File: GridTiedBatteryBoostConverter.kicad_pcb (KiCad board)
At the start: 2 copper layers, 270.1 x 143.1 mm, 161 parts, among them J101 Battery Connection, J103 Solar Panels, J202 Conn_01x03_Female, J203 I2C_BUS, J401 Screw_Terminal_01x02, J402 AudioJack2_SwitchT, Q101 IXFP36N20X3, Q102 BC847B-13-F, Q103 SSM3K329R, Q104 SSM3J334R, Q201 SSM3K329R, Q202 SSM3K329R, Q203 SSM3J334R, Q301 BC847B-13-F, Q302 BC856B-13-F, Q305 TK32A12N1,S4X, Q306 TK32A12N1,S4X, SW201 SW_Up, SW202 SW_Down, SW203 SW_Enter, U101 OPA2837DGK, U102 UCC2800DTR, U201 LCD 2004A, U202 Teensy-LC, U203 PCF8574ADWR, U204 ESP-WROOM-02U, U301 FDA217, U302 LTC7138EMSE-PBF, U303 TPS560200, U304 TLV70430_SOT23-5, U305 REF2925AIDBZT, U306 TPS560200

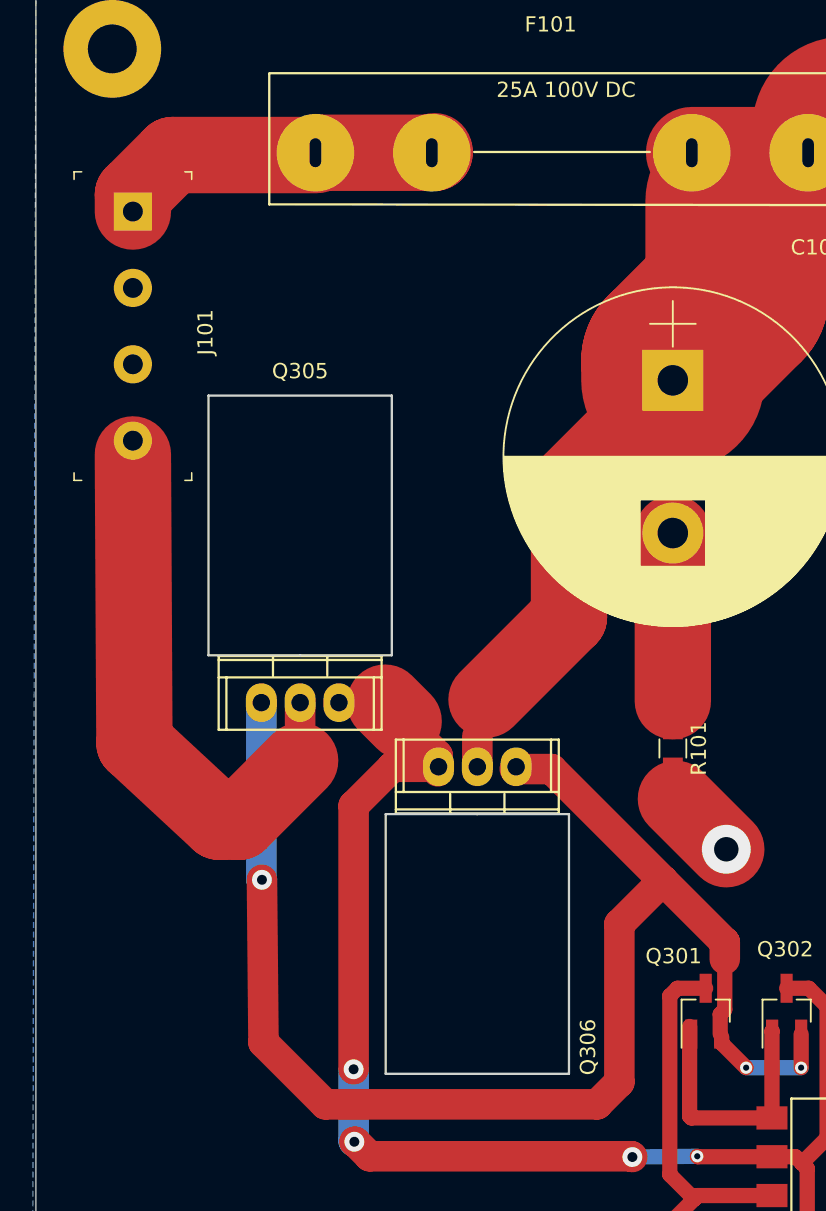
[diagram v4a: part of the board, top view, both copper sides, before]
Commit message: change Fuse details to a graphic note, and change the Fuse supply details to refer to the fuse holder, not the fuse it self.  Also rerouted the charger input using 8mm trace width were possible.
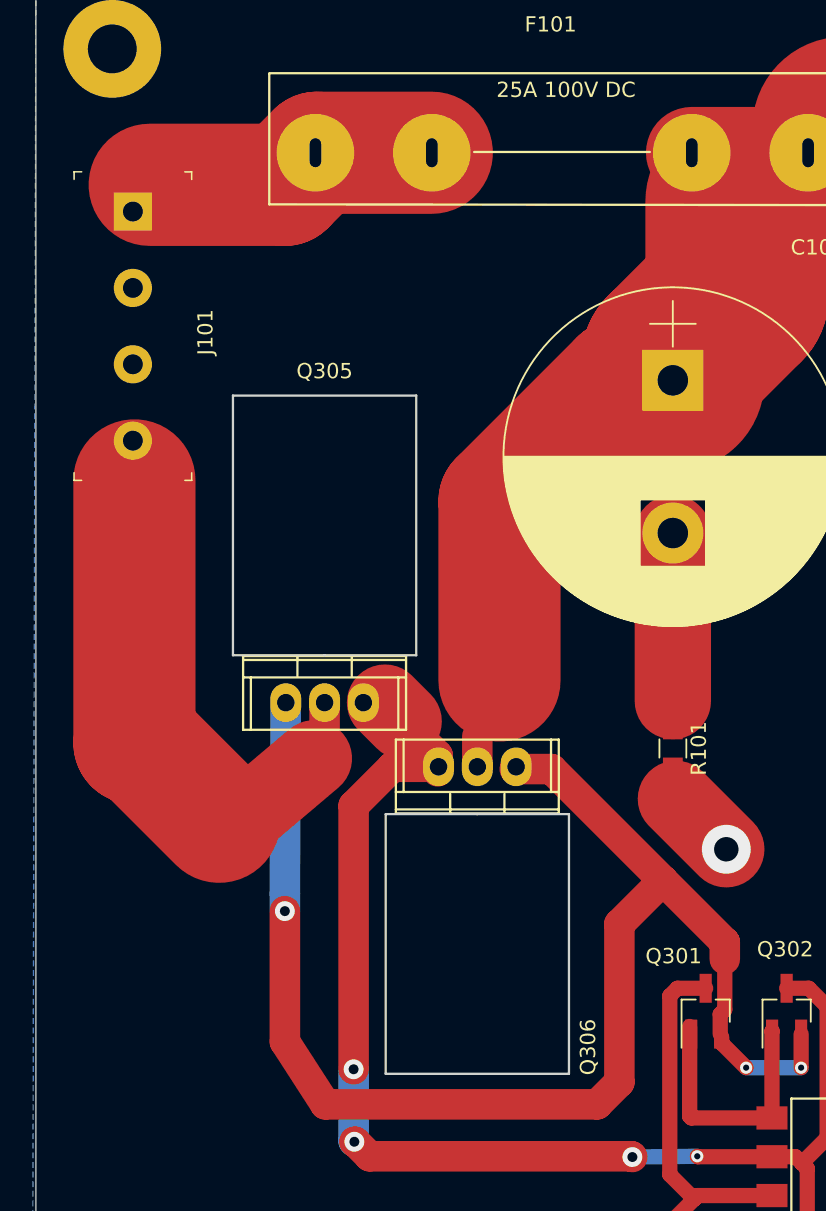
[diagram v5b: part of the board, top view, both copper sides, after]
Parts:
- moved Q305 1.60 mm to (31.9, 62.3)
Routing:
- net Net-(C314-Pad2): track 93.5 -> 90.5 mm
- net Net-(F101-Pad1): track 22.2 -> 19.6 mm
- net ChargerConnection: track 35.2 -> 36.5 mm
- net Net-(Q301-Pad2): track 98.0 -> 97.3 mm

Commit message: added labels for the battery, charger, inverter and solar panels + - connections.
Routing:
- net Vin: track 240.5 -> 244.7 mm
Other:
- board text added: "+ Bat -"
- board text added: "+ Solar Panels -"
- board text added: "- Charger +"

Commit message: Started making progress towards people being able to clone the the repository without getting messages about missing librarys needing rescue. started simplifying where some component librarys are located.
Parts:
- C101: value 220uF 200V 905 mOhm -> 220uF ALUM 200V 905 mOhm 20%
- C102: value 15uF 250VDC 3.9mOhm -> 15uF PP 250VDC 3.9mOhm
- C103: value 470uF 400V 130mOhm -> 470uF ALUM 400V 130mOhm 20%
- C204, C301, C305, C307, C308, C310, C311: value 10uF X7R 16V -> 10uF X7R 25V 10%
- C303, C314: value 1uF X7R 250V -> 1uF X7R 250V 10%
- C306, C315: value 33uF X7R 16V -> 33uF X7R 16V 20%
- D101: value 8A 200V 0.950V fwd -> 8A 200V 0.950V
- D102, D103, D401, D402: value BAV54S -> BAT54S
- F101: value fuse 25A 100V DC -> Fuse Holder
- U101: value OPA2837DGK -> OPA2837IDGKR
- U201: value LCD 2004A -> LCD 2004A Right Angle Header 16 pin 2.54mm
- U303, U306: value TPS560200 -> TPS560200DBVR
- U304: value TLV70430_SOT23-5 -> TLV70430DBVT

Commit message: Changed the ground plane copper fill zone to have a default clearance of 1.25mm to allow for up to 170V for external conductors uncoated according to IPC 2221B Table 6-1.  Then the 500V connectors traces and blocking diodes had clearance set to 2.5mm . Also the thermal relief was set to solid for the zone, which the foot prints inherit.  Minor rerouting for via's that lost access to ground plane due to above clearance changes.  Note the real doc I need should be IEC/UL 60950-1.
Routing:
- net /Vout: track 96.0 -> 83.3 mm
- net 0: track 303.3 -> 311.2 mm, vias 86 -> 87
- net Net-(J103-Pad2): track 107.7 -> 102.8 mm
- net Net-(D101-Pad2): track 105.4 -> 109.0 mm
- net Net-(C112-Pad1): track 48.0 -> 50.4 mm
- net /Vsolar_in: track 26.1 -> 28.2 mm
- net Net-(F101-Pad1): track 19.6 -> 19.0 mm
- net Net-(C105-Pad1): track 16.5 -> 15.9 mm
